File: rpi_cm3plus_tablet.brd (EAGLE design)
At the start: 75.9 x 52.1 mm, 2 parts, among them X1 FH12-15S-0.5SH

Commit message: removed tvdac (should be unused)
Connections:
- net 3.3V: no longer PCB1.166
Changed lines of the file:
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@@
 </signal>
 <signal name="3.3V">
-<contactref element="PCB1" pad="166"/>
 <contactref element="PCB1" pad="194"/>
 <contactref element="PCB1" pad="192"/>
@@
 <wire x1="8.58" y1="40.35" x2="7.98" y2="40.35" width="0" layer="19" extent="1-1"/>
 <wire x1="9.18" y1="40.35" x2="8.58" y2="40.35" width="0" layer="19" extent="1-1"/>
-<wire x1="16.38" y1="40.35" x2="9.18" y2="40.35" width="0" layer="19" extent="1-1"/>
-<wire x1="41.1" y1="7.06" x2="16.38" y2="40.35" width="0" layer="19" extent="1-1"/>
+<wire x1="41.1" y1="7.06" x2="9.18" y2="40.35" width="0" layer="19" extent="1-1"/>
 <wire x1="41.6" y1="7.06" x2="41.1" y2="7.06" width="0" layer="19" extent="1-1"/>
 </signal>

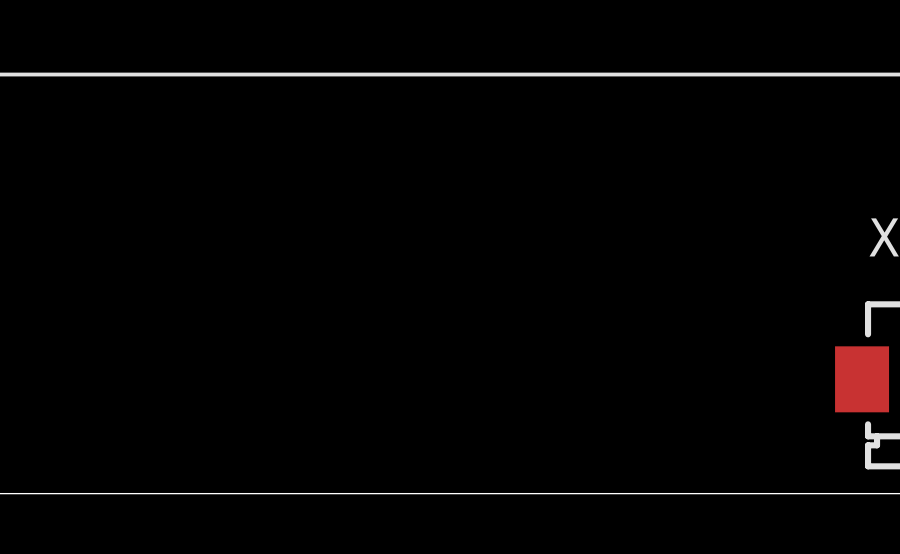
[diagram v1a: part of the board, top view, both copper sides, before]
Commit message: Modified library to include some custom parts and added a basic usb circuit.
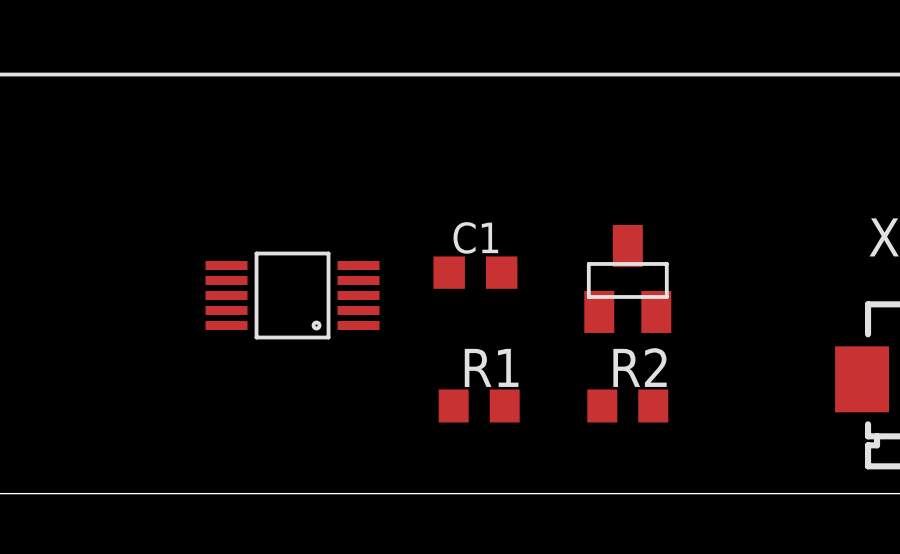
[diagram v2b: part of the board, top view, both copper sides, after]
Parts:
- added C1: 0.1uF, resistor:C0603K
- added R1, R2: 47K, resistor:R0603
- added U$1: FSUSB42MUX, e14_Rpi_Compute_RevC:MSOP-10
- added U$2: BSS138-N, e14_Rpi_Compute_RevC:SOT-23
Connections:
- removed net VBAT: PCB1.197, PCB1.198, PCB1.199, PCB1.200
- new net 5V: PCB1.197, PCB1.198, PCB1.199, PCB1.200, R2.1, U$2.P$1
- new net N$3: C1.2, R1.2, U$1.P$2, U$2.P$3
- new net N$4: U$1.P$9
- new net N$5: U$1.P$8
- new net N$6: U$1.P$7
- new net N$7: U$1.P$6
- new net USB_DM: PCB1.167, U$1.P$4
- new net USB_DP: PCB1.165, U$1.P$3
- net 3.3V: now also C1.1, R1.1, U$1.P$1
- net GND: now also R2.2, U$1.P$10, U$1.P$5, U$2.P$2
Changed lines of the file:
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@@
 <layer number="97" name="Info" color="7" fill="1" visible="no" active="no"/>
 <layer number="98" name="Guide" color="6" fill="1" visible="no" active="no"/>
+<layer number="99" name="SpiceOrder" color="5" fill="1" visible="no" active="no"/>
 <layer number="200" name="200bmp" color="1" fill="10" visible="yes" active="yes"/>
 <layer number="201" name="201bmp" color="2" fill="10" visible="no" active="yes"/>
@@
 <attribute name="OC_NEWARK" value="unknown" x="38.1" y="3.81" size="1.778" layer="27" display="off"/>
 </element>
+<element name="U$1" library="e14_Rpi_Compute_RevC" package="MSOP-10" value="FSUSB42MUX" x="13.716" y="6.604" rot="R90"/>
+<element name="R1" library="resistor" package="R0603" value="47K" x="19.939" y="2.921"/>
+<element name="R2" library="resistor" package="R0603" value="47K" x="24.892" y="2.921"/>
+<element name="C1" library="resistor" package="C0603K" value="0.1uF" x="19.812" y="7.366"/>
+<element name="U$2" library="e14_Rpi_Compute_RevC" package="SOT-23" value="BSS138-N" x="24.892" y="8.255"/>
 </elements>
 <signals>
@@
 <contactref element="X1" pad="13"/>
 <contactref element="PCB1" pad="168"/>
+<contactref element="U$1" pad="P$10"/>
+<contactref element="R2" pad="2"/>
+<contactref element="U$1" pad="P$5"/>
+<contactref element="U$2" pad="P$2"/>
 <wire x1="67.68" y1="48.55" x2="69.48" y2="48.55" width="0" layer="19" extent="1-1"/>
 <wire x1="65.88" y1="48.55" x2="67.68" y2="48.55" width="0" layer="19" extent="1-1"/>
@@
 <wire x1="9.78" y1="40.35" x2="11.58" y2="40.35" width="0" layer="19" extent="1-1"/>
 <wire x1="7.38" y1="40.35" x2="9.78" y2="40.35" width="0" layer="19" extent="1-1"/>
-<wire x1="39.1" y1="7.06" x2="38.58" y2="40.35" width="0" layer="19" extent="1-1"/>
+<wire x1="15.916" y1="7.604" x2="16.98" y2="40.35" width="0" layer="19" extent="1-1"/>
+<wire x1="11.516" y1="5.604" x2="15.916" y2="7.604" width="0" layer="19" extent="1-1"/>
+<wire x1="25.842" y1="6.055" x2="11.516" y2="5.604" width="0" layer="19" extent="1-1"/>
+<wire x1="25.742" y1="2.921" x2="15.916" y2="7.604" width="0" layer="19" extent="1-1"/>
+<wire x1="34.6" y1="7.06" x2="25.742" y2="2.921" width="0" layer="19" extent="1-1"/>
+<wire x1="36.1" y1="7.06" x2="34.6" y2="7.06" width="0" layer="19" extent="1-1"/>
+<wire x1="37.6" y1="7.06" x2="36.1" y2="7.06" width="0" layer="19" extent="1-1"/>
+<wire x1="39.1" y1="7.06" x2="37.6" y2="7.06" width="0" layer="19" extent="1-1"/>
 <wire x1="40.6" y1="7.06" x2="39.1" y2="7.06" width="0" layer="19" extent="1-1"/>
-<wire x1="37.6" y1="7.06" x2="39.1" y2="7.06" width="0" layer="19" extent="1-1"/>
-<wire x1="36.1" y1="7.06" x2="37.6" y2="7.06" width="0" layer="19" extent="1-1"/>
-<wire x1="34.6" y1="7.06" x2="36.1" y2="7.06" width="0" layer="19" extent="1-1"/>
-</signal>
-<signal name="VBAT">
-<contactref element="PCB1" pad="198"/>
-<contactref element="PCB1" pad="200"/>
-<contactref element="PCB1" pad="197"/>
-<contactref element="PCB1" pad="199"/>
-<wire x1="6.48" y1="48.55" x2="7.08" y2="48.55" width="0" layer="19" extent="1-1"/>
-<wire x1="6.78" y1="40.35" x2="7.08" y2="48.55" width="0" layer="19" extent="1-1"/>
-<wire x1="6.18" y1="40.35" x2="6.78" y2="40.35" width="0" layer="19" extent="1-1"/>
 </signal>
 <signal name="1.8V">
@@
 <contactref element="X1" pad="15"/>
 <contactref element="X1" pad="14"/>
+<contactref element="U$1" pad="P$1"/>
+<contactref element="R1" pad="1"/>
+<contactref element="C1" pad="1"/>
 <wire x1="8.28" y1="48.55" x2="8.88" y2="48.55" width="0" layer="19" extent="1-1"/>
 <wire x1="9.48" y1="48.55" x2="8.88" y2="48.55" width="0" layer="19" extent="1-1"/>
@@
 <wire x1="8.58" y1="40.35" x2="7.98" y2="40.35" width="0" layer="19" extent="1-1"/>
 <wire x1="9.18" y1="40.35" x2="8.58" y2="40.35" width="0" layer="19" extent="1-1"/>
-<wire x1="41.1" y1="7.06" x2="9.18" y2="40.35" width="0" layer="19" extent="1-1"/>
+<wire x1="18.937" y1="7.366" x2="9.18" y2="40.35" width="0" layer="19" extent="1-1"/>
+<wire x1="15.916" y1="5.604" x2="18.937" y2="7.366" width="0" layer="19" extent="1-1"/>
+<wire x1="19.089" y1="2.921" x2="15.916" y2="5.604" width="0" layer="19" extent="1-1"/>
+<wire x1="41.1" y1="7.06" x2="18.937" y2="7.366" width="0" layer="19" extent="1-1"/>
 <wire x1="41.6" y1="7.06" x2="41.1" y2="7.06" width="0" layer="19" extent="1-1"/>
 </signal>
@@
 <wire x1="40.1" y1="7.06" x2="68.88" y2="48.55" width="0" layer="19" extent="1-1"/>
 </signal>
+<signal name="N$3">
+<contactref element="U$1" pad="P$2"/>
+<contactref element="R1" pad="2"/>
+<contactref element="C1" pad="2"/>
+<contactref element="U$2" pad="P$3"/>
+<wire x1="20.789" y1="2.921" x2="20.687" y2="7.366" width="0" layer="19" extent="1-1"/>
+<wire x1="15.916" y1="6.104" x2="20.687" y2="7.366" width="0" layer="19" extent="1-1"/>
+<wire x1="24.892" y1="8.255" x2="15.916" y2="6.104" width="0" layer="19" extent="1-1"/>
+</signal>
+<signal name="N$4">
+<contactref element="U$1" pad="P$9"/>
+</signal>
+<signal name="N$5">
+<contactref element="U$1" pad="P$8"/>
+</signal>
+<signal name="N$6">
+<contactref element="U$1" pad="P$7"/>
+</signal>
+<signal name="N$7">
+<contactref element="U$1" pad="P$6"/>
+</signal>
+<signal name="USB_DP">
+<contactref element="PCB1" pad="165"/>
+<contactref element="U$1" pad="P$3"/>
+<wire x1="15.916" y1="6.604" x2="16.68" y2="48.55" width="0" layer="19" extent="1-1"/>
+</signal>
+<signal name="USB_DM">
+<contactref element="PCB1" pad="167"/>
+<contactref element="U$1" pad="P$4"/>
+<wire x1="15.916" y1="7.104" x2="16.08" y2="48.55" width="0" layer="19" extent="1-1"/>
+</signal>
+<signal name="5V">
+<contactref element="R2" pad="1"/>
+<contactref element="PCB1" pad="198"/>
+<contactref element="PCB1" pad="200"/>
+<contactref element="PCB1" pad="197"/>
+<contactref element="PCB1" pad="199"/>
+<contactref element="U$2" pad="P$1"/>
+<wire x1="6.48" y1="48.55" x2="7.08" y2="48.55" width="0" layer="19" extent="1-1"/>
+<wire x1="6.78" y1="40.35" x2="7.08" y2="48.55" width="0" layer="19" extent="1-1"/>
+<wire x1="6.18" y1="40.35" x2="6.78" y2="40.35" width="0" layer="19" extent="1-1"/>
+<wire x1="23.942" y1="6.055" x2="6.18" y2="40.35" width="0" layer="19" extent="1-1"/>
+<wire x1="24.042" y1="2.921" x2="23.942" y2="6.055" width="0" layer="19" extent="1-1"/>
+</signal>
 </signals>

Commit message: further updates to schematic regarding custom library
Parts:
- PCB1: device e14_Rpi_Compute_RevC:RPI_COMPUTE -> rpi_cm3plus_tablet:RPI_COMPUTE
- U$1: device e14_Rpi_Compute_RevC:MSOP-10 -> rpi_cm3plus_tablet:MSOP-10
- U$2: value BSS138-N -> BSS138N; device e14_Rpi_Compute_RevC:SOT-23 -> rpi_cm3plus_tablet:SOT-23
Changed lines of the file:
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@@
 </autorouter>
 <elements>
-<element name="PCB1" library="e14_Rpi_Compute_RevC" package="RPI_COMPUTE" value="RPI_COMPUTE" x="38.1" y="44.45" rot="R180"/>
+<element name="PCB1" library="rpi_cm3plus_tablet" package="RPI_COMPUTE" value="RPI_COMPUTE" x="38.1" y="44.45" rot="R180"/>
 <element name="X1" library="con-hirose" package="FH12-15S-0.5SH" value="FH12-15S-0.5SH" x="38.1" y="3.81">
 <attribute name="OC_FARNELL" value="1324545" x="38.1" y="3.81" size="1.778" layer="27" display="off"/>
@@
 <attribute name="OC_NEWARK" value="unknown" x="38.1" y="3.81" size="1.778" layer="27" display="off"/>
 </element>
-<element name="U$1" library="e14_Rpi_Compute_RevC" package="MSOP-10" value="FSUSB42MUX" x="13.716" y="6.604" rot="R90"/>
+<element name="U$1" library="rpi_cm3plus_tablet" package="MSOP-10" value="FSUSB42MUX" x="13.716" y="6.604" rot="R90"/>
 <element name="R1" library="resistor" package="R0603" value="47K" x="19.939" y="2.921"/>
 <element name="R2" library="resistor" package="R0603" value="47K" x="24.892" y="2.921"/>
 <element name="C1" library="resistor" package="C0603K" value="0.1uF" x="19.812" y="7.366"/>
-<element name="U$2" library="e14_Rpi_Compute_RevC" package="SOT-23" value="BSS138-N" x="24.892" y="8.255"/>
+<element name="U$2" library="rpi_cm3plus_tablet" package="SOT-23" value="BSS138N" x="24.892" y="8.255"/>
 </elements>
 <signals>
